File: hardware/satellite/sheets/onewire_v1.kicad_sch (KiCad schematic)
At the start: 5 parts, among them J6 Conn_01x03, U3 DS2482S-100+

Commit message: fix(satellite): Consolidate shared libraries, fix MDX/links, and update JST PA LCSC part (#24)
* Consolidate Hub and Satellite libraries into shared hardware/libraries

* Add SunSprout logo to Satellite silkscreen and refresh documentation assets

* Fix MDX compilation error and broken links in satellite documentation

* Update DS18B20 and moisture probe connectors to JST PA with LCSC part C131339
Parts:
- J6: LCSC Part C265095 -> C131339
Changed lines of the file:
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@@
 			)
 		)
-		(property "LCSC Part" "C265095"
+		(property "LCSC Part" "C131339"
 			(at 203.2 76.2 0)
 			(hide yes)

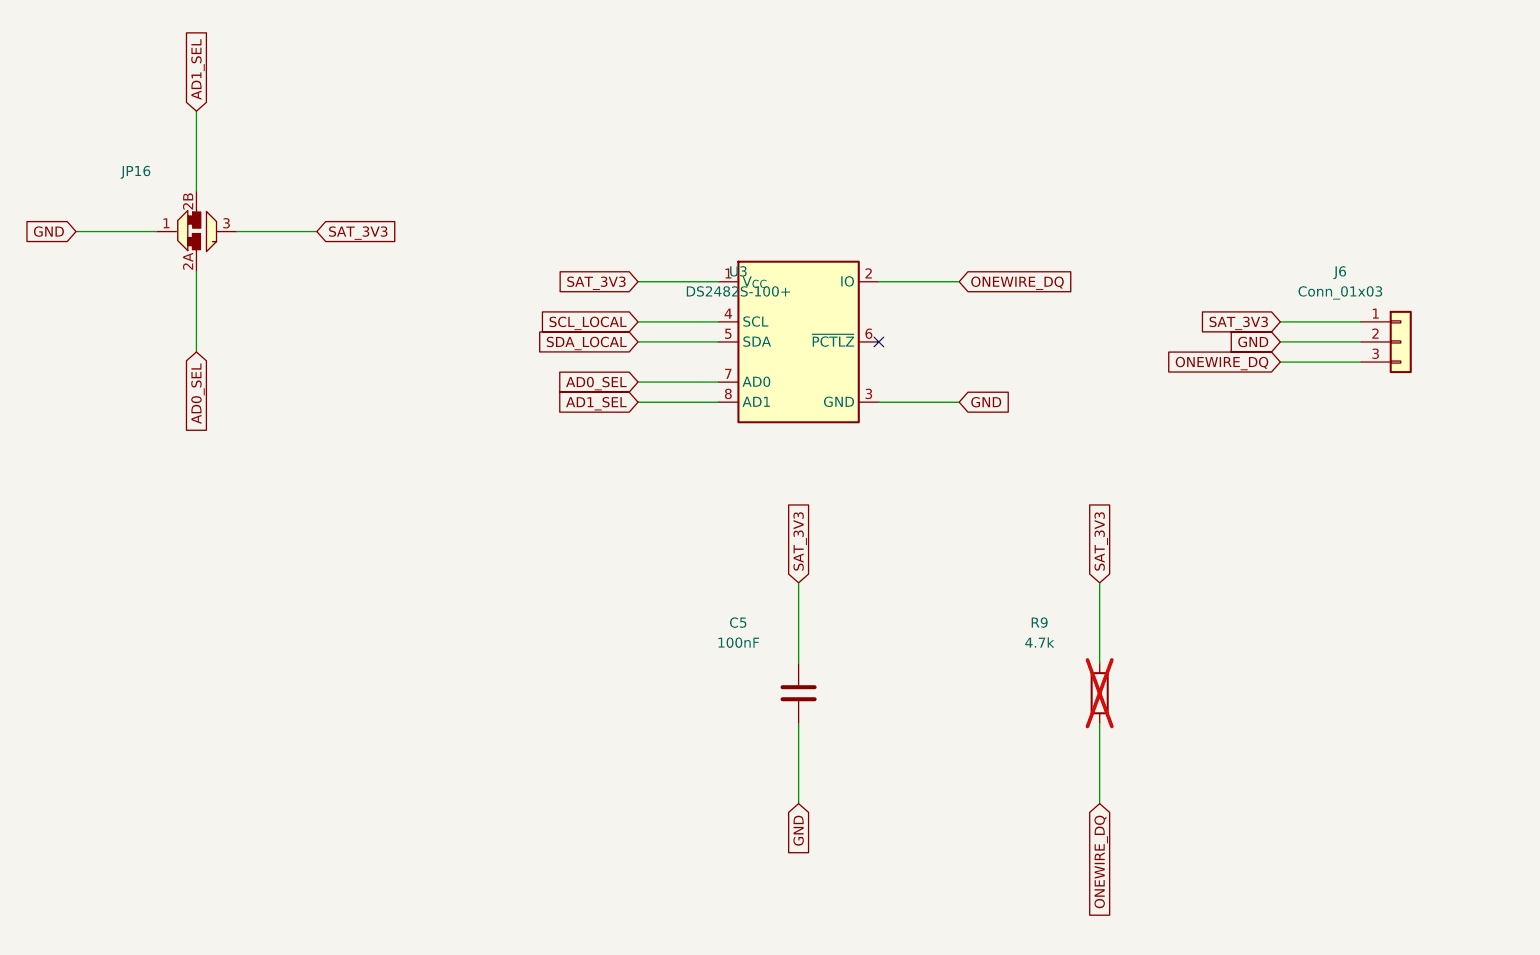
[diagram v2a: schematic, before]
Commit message: feat(satellite): redesign power entry architecture, solder jumpers, and address footprints
- Decouple raw cable power (Pair 1: RJ45_VCC_1/GND_1, Pair 3: RJ45_VCC_2/GND_2) onto 4P header J7
- Add 2P header J9 for local satellite power (SAT_3V3, GND) to support external regulation
- Add normally-closed cuttable jumpers JP18 (VCC_1 <-> SAT_3V3) and JP17 (GND_1 <-> GND)
- Tie PCA9615 VDDB, diff termination bias (R3/R5/R6/R8), and TVS U4 to RJ45_VCC_1/GND_1
- Place bulk cap C1 (22uF) across RJ45_VCC_1 and RJ45_GND_1 at cable entry
- Split inner planes: continuous RJ45_GND_1 reference on In2.Cu under B.Cu diff pairs; In1.Cu split (SAT GND, RJ45 GND, VCC2)
- Update 1-Wire address jumper footprint with +1/+2 bit-weighting notation and 0x18 default
- Remove deprecated pcb-pipeline generator scripts
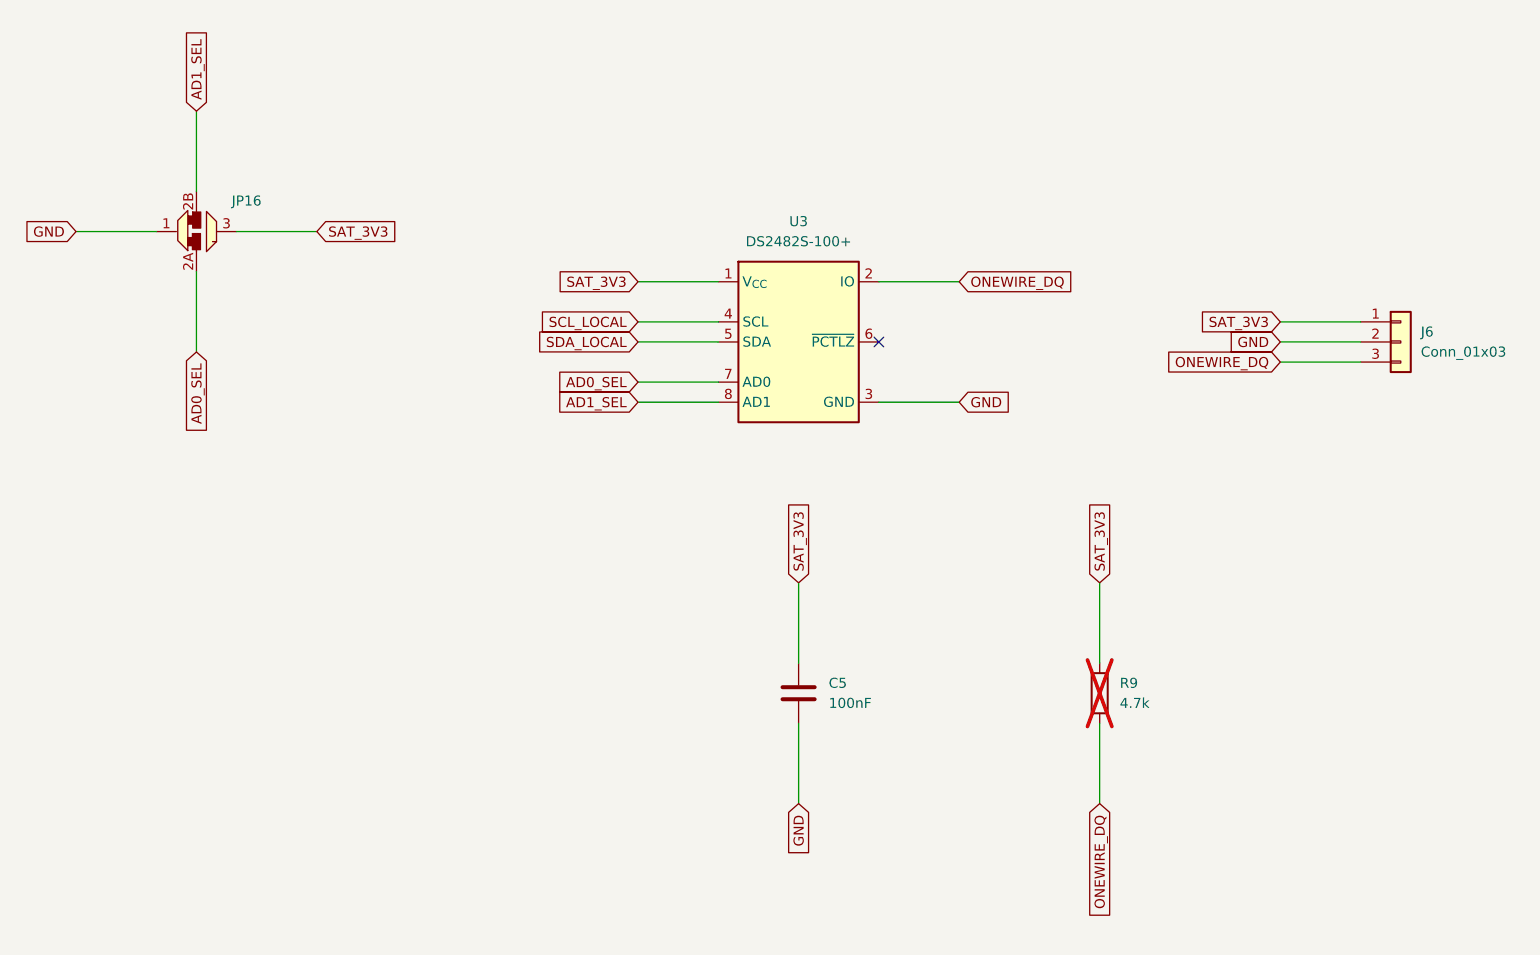
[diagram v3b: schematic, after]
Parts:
- C5: footprint Capacitor_SMD:C_0603_1608Metric -> Capacitor_SMD:C_0805_2012Metric_Pad1.18x1.45mm_HandSolder; LCSC Part C14663 -> C28233
- JP16: footprint project:SolderJumper-3_P1.3mm_DualAddrSelect_RoundedPad1.0x1.5mm -> project:SolderJumper-3_P_1WAddr

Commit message: Fixed missed 603 component that was marked DNP
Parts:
- R9: footprint Resistor_SMD:R_0603_1608Metric -> Resistor_SMD:R_0805_2012Metric_Pad1.20x1.40mm_HandSolder
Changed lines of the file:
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@@
 			)
 		)
-		(property "Footprint" "Resistor_SMD:R_0603_1608Metric"
+		(property "Footprint" "Resistor_SMD:R_0805_2012Metric_Pad1.20x1.40mm_HandSolder"
 			(at 165.1 120.65 0)
 			(hide yes)
